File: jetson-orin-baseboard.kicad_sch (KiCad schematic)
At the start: 4 parts

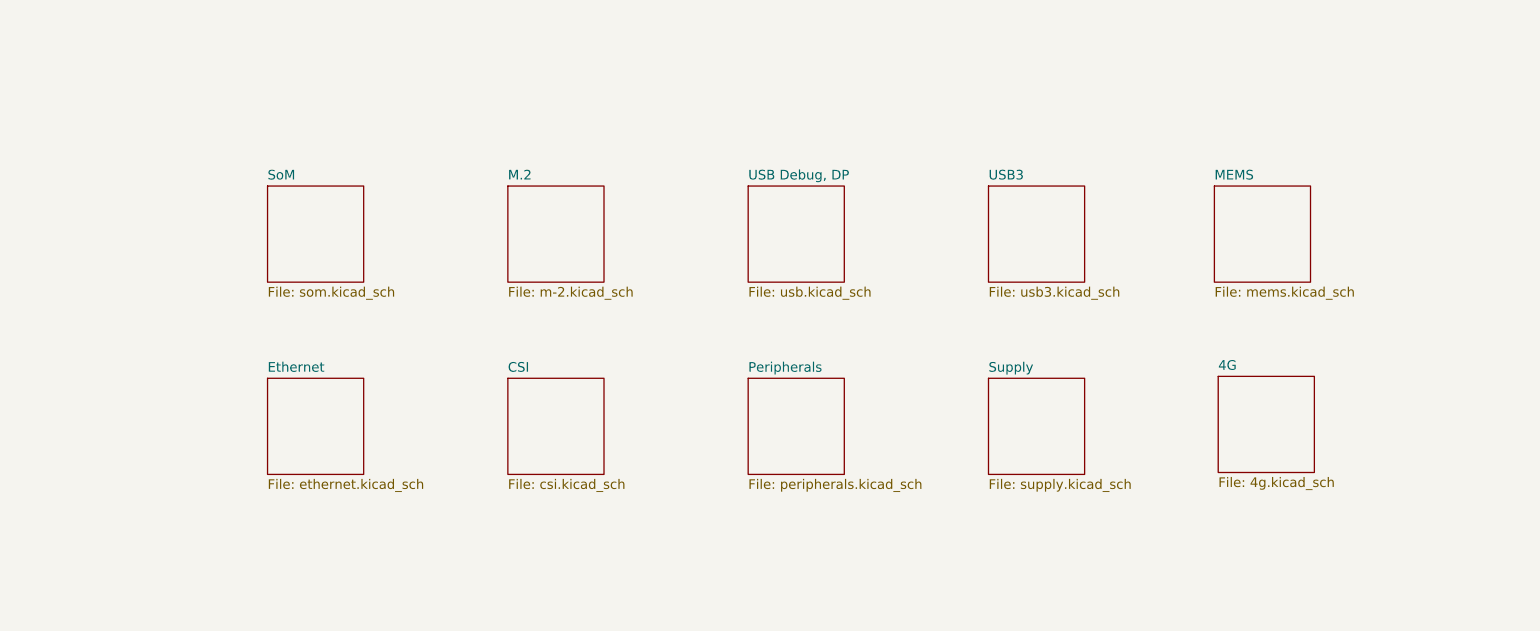
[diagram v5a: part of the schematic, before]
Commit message: Adding 4G M.2 B
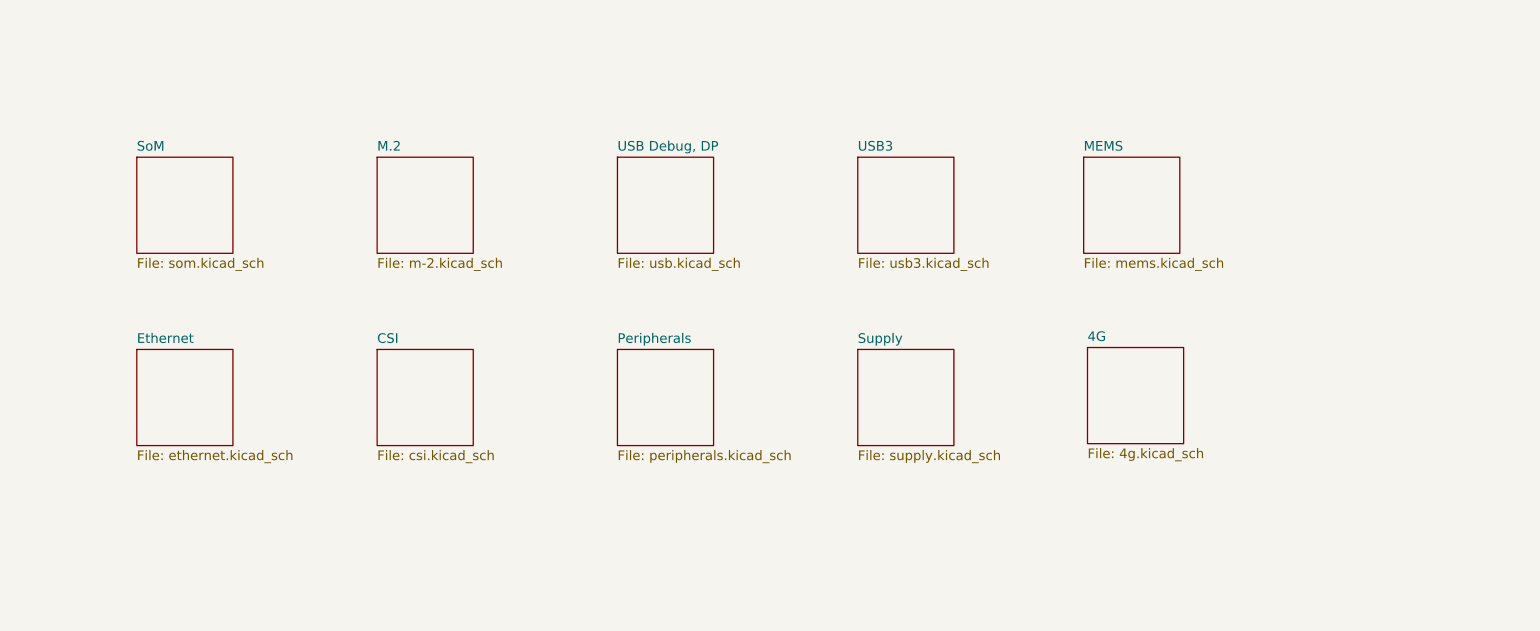
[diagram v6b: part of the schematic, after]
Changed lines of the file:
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@@
     )
   )
-  (sheet (at 283.083 210.566) (size 12.7 12.7) (fields_autoplaced)
+  (sheet (at 265.811 206.756) (size 12.7 12.7) (fields_autoplaced)
     (stroke (width 0.1524) (type solid))
     (fill (color 0 0 0 0.0000))
-    (property "Sheetname" "4G" (at 283.083 209.8544 0)
+    (property "Sheetname" "4G" (at 265.811 206.0444 0)
       (effects (font (size 1.27 1.27)) (justify left bottom))
     )
-    (property "Sheetfile" "4g.kicad_sch" (at 283.083 223.8506 0)
+    (property "Sheetfile" "4g.kicad_sch" (at 265.811 220.0406 0)
       (effects (font (size 1.27 1.27)) (justify left top))
     )
@@
     )
   )
-  (sheet (at 282.575 185.42) (size 12.7 12.7) (fields_autoplaced)
+  (sheet (at 265.303 181.61) (size 12.7 12.7) (fields_autoplaced)
     (stroke (width 0.1524) (type solid))
     (fill (color 0 0 0 0.0000))
-    (property "Sheetname" "MEMS" (at 282.575 184.7084 0)
+    (property "Sheetname" "MEMS" (at 265.303 180.8984 0)
       (effects (font (size 1.27 1.27)) (justify left bottom))
     )
-    (property "Sheetfile" "mems.kicad_sch" (at 282.575 198.7046 0)
+    (property "Sheetfile" "mems.kicad_sch" (at 265.303 194.8946 0)
       (effects (font (size 1.27 1.27)) (justify left top))
     )
@@
     )
   )
-  (sheet (at 252.73 185.42) (size 12.7 12.7) (fields_autoplaced)
+  (sheet (at 235.458 181.61) (size 12.7 12.7) (fields_autoplaced)
     (stroke (width 0.1524) (type solid))
     (fill (color 0 0 0 0.0000))
-    (property "Sheetname" "USB3" (at 252.73 184.7084 0)
+    (property "Sheetname" "USB3" (at 235.458 180.8984 0)
       (effects (font (size 1.27 1.27)) (justify left bottom))
     )
-    (property "Sheetfile" "usb3.kicad_sch" (at 252.73 198.7046 0)
+    (property "Sheetfile" "usb3.kicad_sch" (at 235.458 194.8946 0)
       (effects (font (size 1.27 1.27)) (justify left top))
     )
@@
     )
   )
-  (sheet (at 252.73 210.82) (size 12.7 12.7) (fields_autoplaced)
+  (sheet (at 235.458 207.01) (size 12.7 12.7) (fields_autoplaced)
     (stroke (width 0.1524) (type solid))
     (fill (color 0 0 0 0.0000))
-    (property "Sheetname" "Supply" (at 252.73 210.1084 0)
+    (property "Sheetname" "Supply" (at 235.458 206.2984 0)
       (effects (font (size 1.27 1.27)) (justify left bottom))
     )
-    (property "Sheetfile" "supply.kicad_sch" (at 252.73 224.1046 0)
+    (property "Sheetfile" "supply.kicad_sch" (at 235.458 220.2946 0)
       (effects (font (size 1.27 1.27)) (justify left top))
     )
@@
     )
   )
-  (sheet (at 157.48 185.42) (size 12.7 12.7) (fields_autoplaced)
+  (sheet (at 140.208 181.61) (size 12.7 12.7) (fields_autoplaced)
     (stroke (width 0.1524) (type solid))
     (fill (color 0 0 0 0.0000))
-    (property "Sheetname" "SoM" (at 157.48 184.7084 0)
+    (property "Sheetname" "SoM" (at 140.208 180.8984 0)
       (effects (font (size 1.27 1.27)) (justify left bottom))
     )
-    (property "Sheetfile" "som.kicad_sch" (at 157.48 198.7046 0)
+    (property "Sheetfile" "som.kicad_sch" (at 140.208 194.8946 0)
       (effects (font (size 1.27 1.27)) (justify left top))
     )
@@
     )
   )
-  (sheet (at 189.23 210.82) (size 12.7 12.7) (fields_autoplaced)
+  (sheet (at 171.958 207.01) (size 12.7 12.7) (fields_autoplaced)
     (stroke (width 0.1524) (type solid))
     (fill (color 0 0 0 0.0000))
-    (property "Sheetname" "CSI" (at 189.23 210.1084 0)
+    (property "Sheetname" "CSI" (at 171.958 206.2984 0)
       (effects (font (size 1.27 1.27)) (justify left bottom))
     )
-    (property "Sheetfile" "csi.kicad_sch" (at 189.23 224.1046 0)
+    (property "Sheetfile" "csi.kicad_sch" (at 171.958 220.2946 0)
       (effects (font (size 1.27 1.27)) (justify left top))
     )
@@
     )
   )
-  (sheet (at 189.23 185.42) (size 12.7 12.7) (fields_autoplaced)
+  (sheet (at 171.958 181.61) (size 12.7 12.7) (fields_autoplaced)
     (stroke (width 0.1524) (type solid))
     (fill (color 0 0 0 0.0000))
-    (property "Sheetname" "M.2" (at 189.23 184.7084 0)
+    (property "Sheetname" "M.2" (at 171.958 180.8984 0)
       (effects (font (size 1.27 1.27)) (justify left bottom))
     )
-    (property "Sheetfile" "m-2.kicad_sch" (at 189.23 198.7046 0)
+    (property "Sheetfile" "m-2.kicad_sch" (at 171.958 194.8946 0)
       (effects (font (size 1.27 1.27)) (justify left top))
     )
@@
     )
   )
-  (sheet (at 157.48 210.82) (size 12.7 12.7) (fields_autoplaced)
+  (sheet (at 140.208 207.01) (size 12.7 12.7) (fields_autoplaced)
     (stroke (width 0.1524) (type solid))
     (fill (color 0 0 0 0.0000))
-    (property "Sheetname" "Ethernet" (at 157.48 210.1084 0)
+    (property "Sheetname" "Ethernet" (at 140.208 206.2984 0)
       (effects (font (size 1.27 1.27)) (justify left bottom))
     )
-    (property "Sheetfile" "ethernet.kicad_sch" (at 157.48 224.1046 0)
+    (property "Sheetfile" "ethernet.kicad_sch" (at 140.208 220.2946 0)
       (effects (font (size 1.27 1.27)) (justify left top))
     )
@@
     )
   )
-  (sheet (at 220.98 210.82) (size 12.7 12.7) (fields_autoplaced)
+  (sheet (at 203.708 207.01) (size 12.7 12.7) (fields_autoplaced)
     (stroke (width 0.1524) (type solid))
     (fill (color 0 0 0 0.0000))
-    (property "Sheetname" "Peripherals" (at 220.98 210.1084 0)
+    (property "Sheetname" "Peripherals" (at 203.708 206.2984 0)
       (effects (font (size 1.27 1.27)) (justify left bottom))
     )
-    (property "Sheetfile" "peripherals.kicad_sch" (at 220.98 224.1046 0)
+    (property "Sheetfile" "peripherals.kicad_sch" (at 203.708 220.2946 0)
       (effects (font (size 1.27 1.27)) (justify left top))
     )
@@
     )
   )
-  (sheet (at 220.98 185.42) (size 12.7 12.7) (fields_autoplaced)
+  (sheet (at 203.708 181.61) (size 12.7 12.7) (fields_autoplaced)
     (stroke (width 0.1524) (type solid))
     (fill (color 0 0 0 0.0000))
-    (property "Sheetname" "USB Debug, DP" (at 220.98 184.7084 0)
+    (property "Sheetname" "USB Debug, DP" (at 203.708 180.8984 0)
       (effects (font (size 1.27 1.27)) (justify left bottom))
     )
-    (property "Sheetfile" "usb.kicad_sch" (at 220.98 198.7046 0)
+    (property "Sheetfile" "usb.kicad_sch" (at 203.708 194.8946 0)
       (effects (font (size 1.27 1.27)) (justify left top))
     )
